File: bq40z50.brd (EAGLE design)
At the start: 148 x 13 mm, 46 parts, among them Q1 6.5A/30V/38mΩ, Q2 6.5A/30V/38mΩ, U1 BQ40Z50RSMTRSM32_1P5X1P5-M

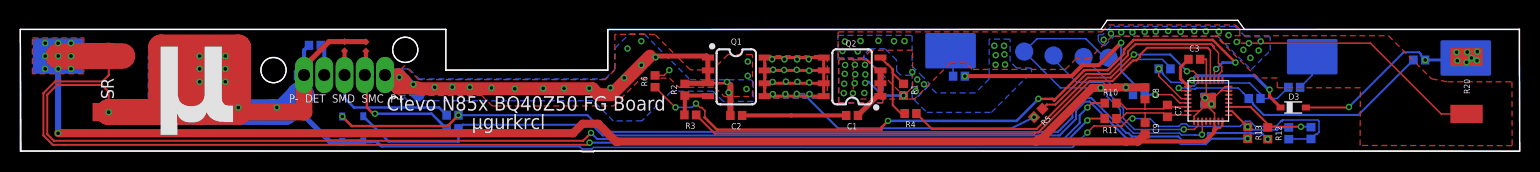
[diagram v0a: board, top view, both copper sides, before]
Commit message: board : apply schematic changes
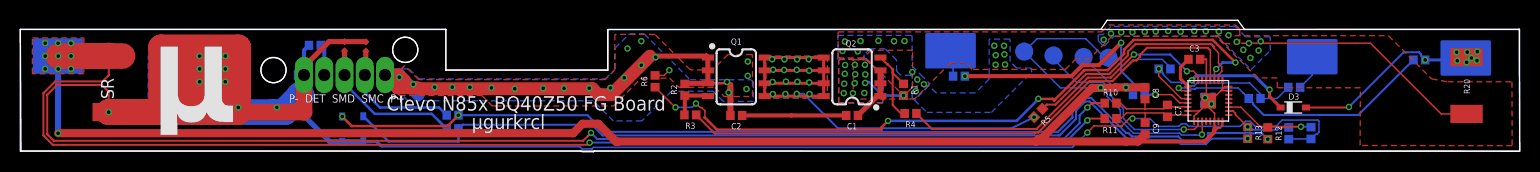
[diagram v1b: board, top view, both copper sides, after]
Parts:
- D3: value BAT60J -> (none)
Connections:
- net GND: now also U1.25
- net N$28: now also SG1.1, U$1.SMBD; no longer SG2.1, U$1.SMBC
- net N$29: now also SG2.1, U$1.SMBC; no longer SG1.1, U$1.SMBD
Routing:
- net N$29: track 15.4 -> 13.1 mm
- net GND: track 314.7 -> 315.6 mm
- net N$28: track 14.4 -> 15.2 mm, vias 1 -> 0
- added copper zone on layer 16, net N$32
- removed copper zone on layer 16, net N$3
